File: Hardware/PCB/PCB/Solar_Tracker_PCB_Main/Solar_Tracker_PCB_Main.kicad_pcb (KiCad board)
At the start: 4 copper layers, 95.4 x 96.8 mm, 59 parts, among them IC1 ESP32-S3-WROOM-1-N4R8, IC2 TPS54302DDCT, IC3 BNO085, IC4 PCF2131TFY, IC5 LM1117MPX-3.3_NOPB, J1 1729076, J2 USB4940-00-A, J3 1729076, J4 1977223-1, J5 1977223-1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

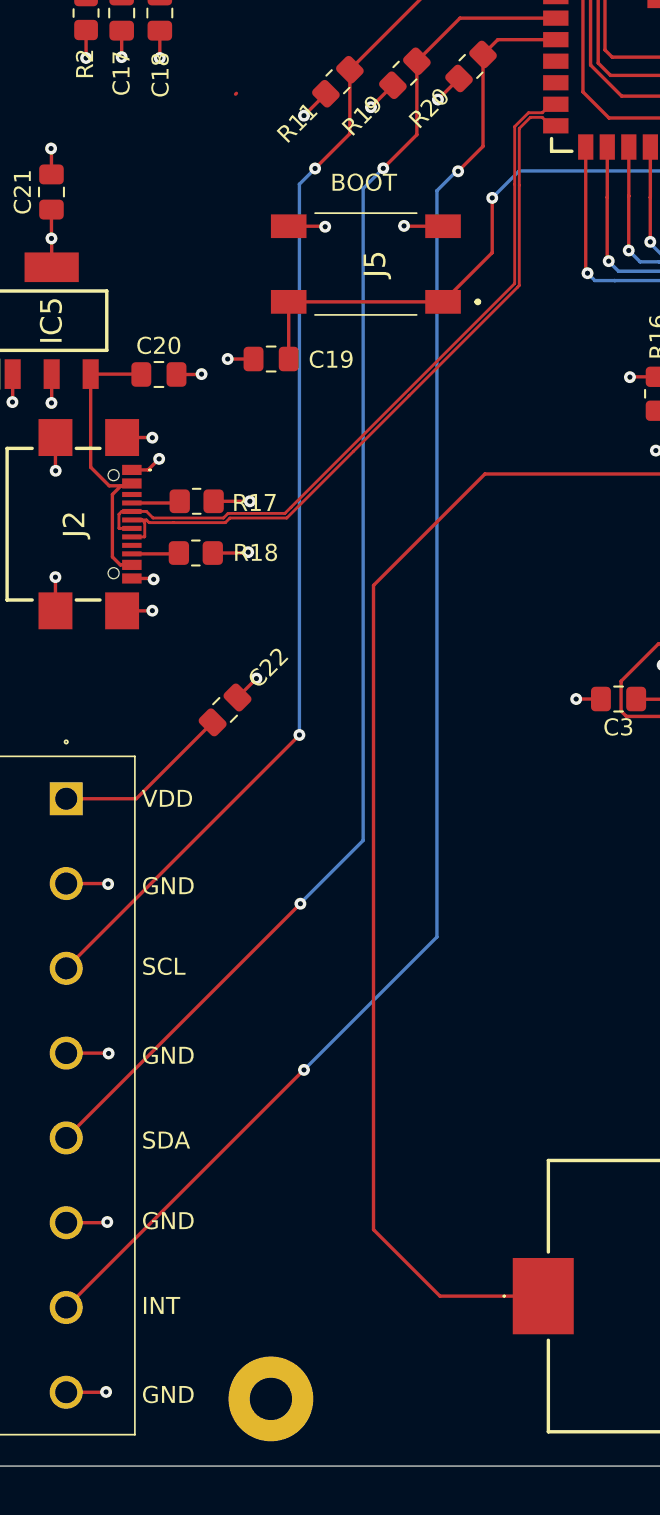
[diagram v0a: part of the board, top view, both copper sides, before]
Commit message: Confi del par diferencial
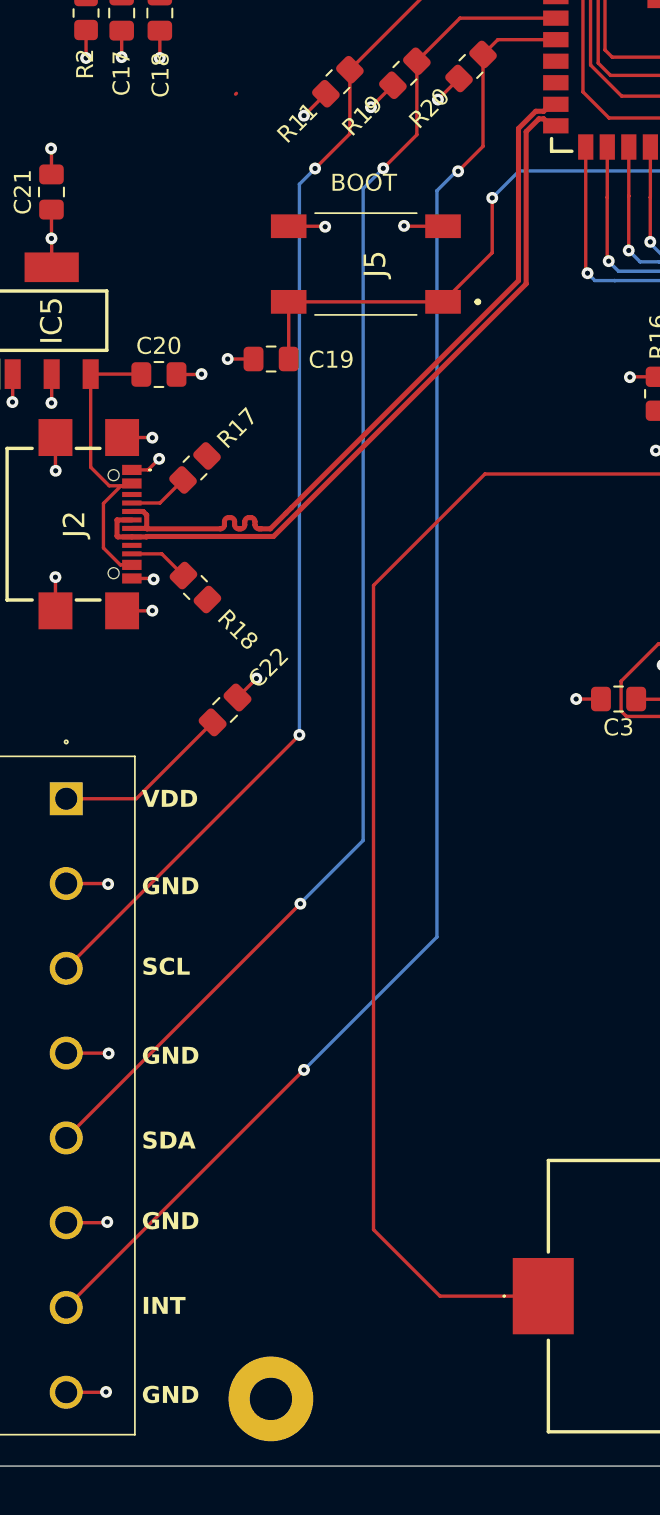
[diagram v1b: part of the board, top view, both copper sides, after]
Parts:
- moved R18 2.04 mm to (84.5, 89.5), turned to -45 degrees
- moved R17 1.97 mm to (84.5, 82.4), turned to -135 degrees
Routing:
- net GND: track 108.0 -> 103.7 mm, vias 44 -> 42
- net D-: track 43.1 -> 44.1 mm
- net Net-(J2-CC2): track 2.79 -> 3.57 mm
- net Net-(J2-CC1): track 2.86 -> 3.58 mm

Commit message: Par deferencial
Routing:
- net D-: track 44.1 -> 43.6 mm
